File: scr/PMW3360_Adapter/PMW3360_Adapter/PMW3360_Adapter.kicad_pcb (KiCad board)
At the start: 2 copper layers, 11 parts, among them J1 Conn_01x06_Female, J2 Conn_01x02_Male, U1 TLV70019_SOT23-5, U2 PMW3360

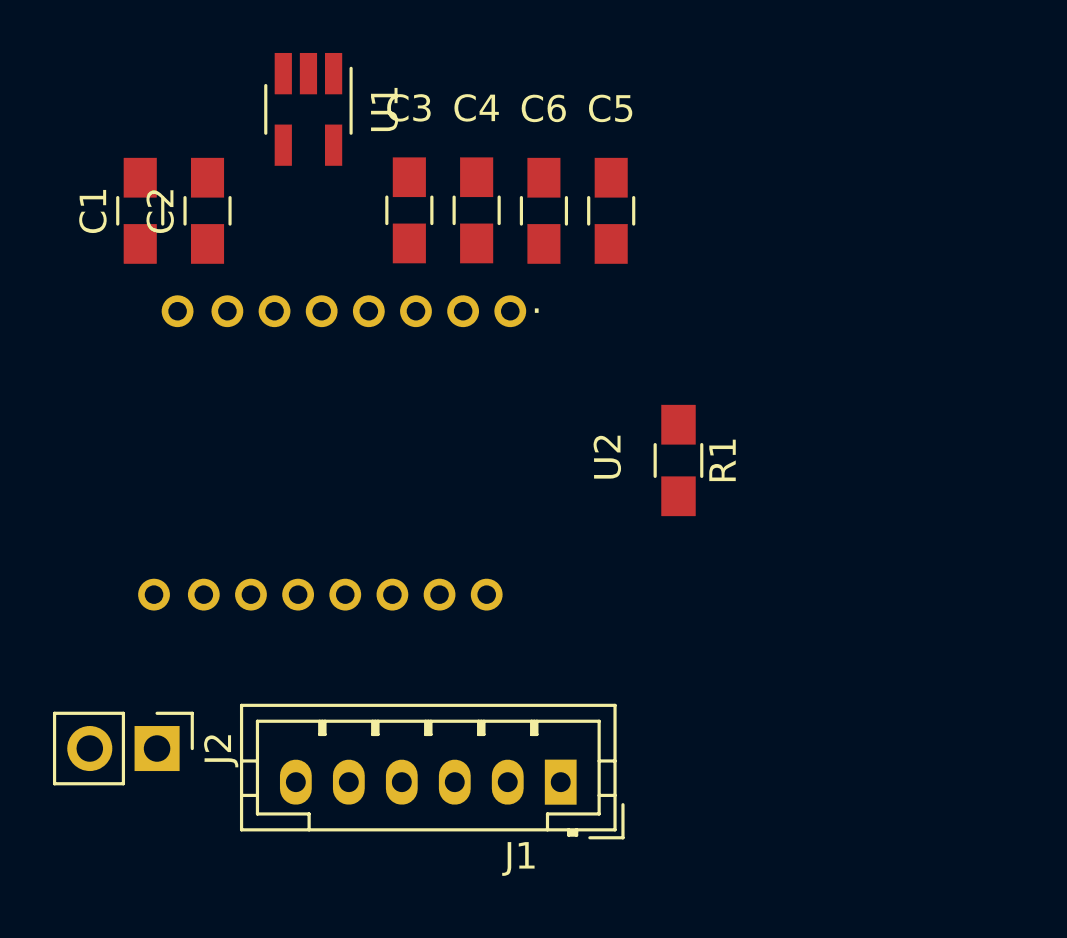
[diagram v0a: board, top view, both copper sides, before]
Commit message: PMW3360 Breakout ordered
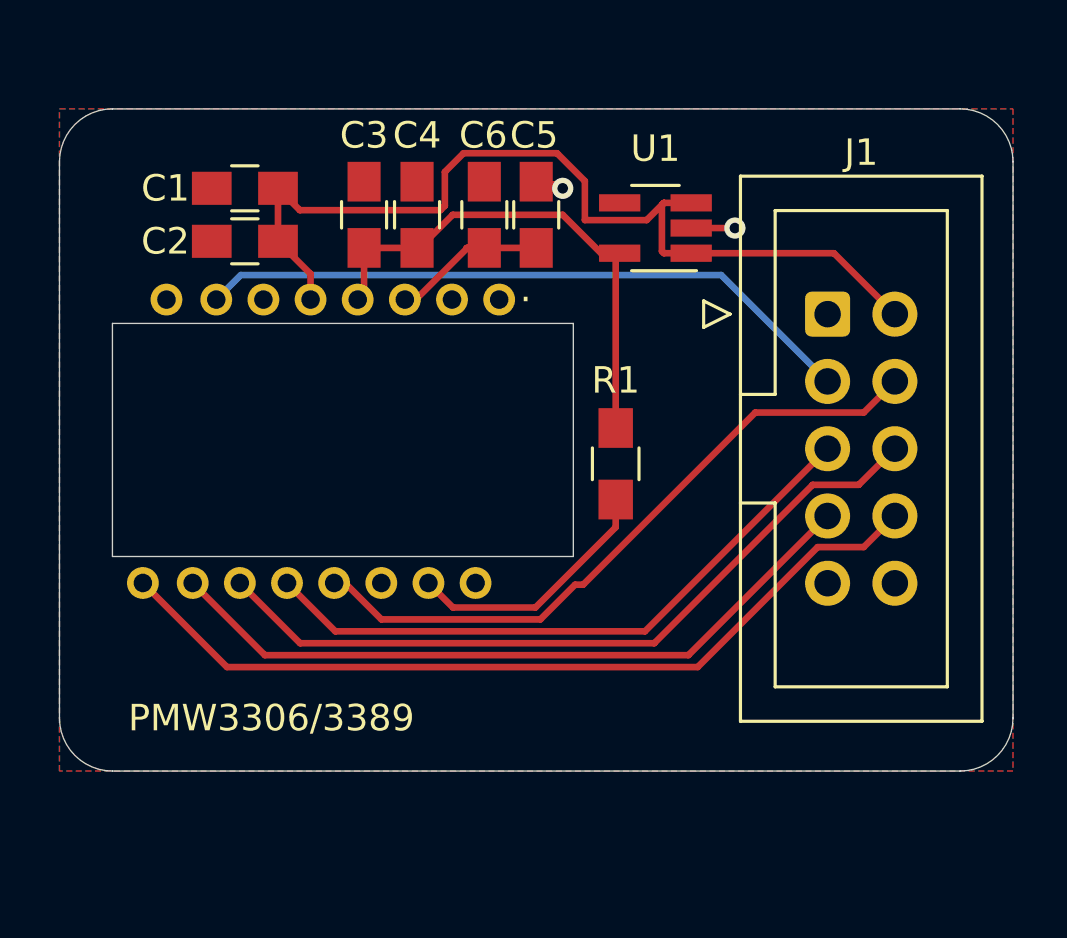
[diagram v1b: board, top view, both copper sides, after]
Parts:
- removed J2: Conn_01x02_Male, Pin_Headers:Pin_Header_Straight_1x02_Pitch2.54mm
- J1: value Conn_01x06_Female -> Conn_02x05_Odd_Even; footprint Connectors_JST:JST_PH_B6B-PH-K_06x2.00mm_Straight -> Connector_IDC:IDC-Header_2x05_P2.54mm_Vertical
- moved J1 20.3 mm to (108.5, 40.8), turned to 0 degrees
- moved U1 13.8 mm to (102.0, 37.5), turned to 180 degrees
- moved C1 4.04 mm to (86.5, 36.0), turned to 180 degrees
- moved C5 2.83 mm to (97.5, 37.0)
- moved R1 2.37 mm to (100.5, 46.4)
- moved C4 2.26 mm to (93.0, 37.0)
- moved C6 2.25 mm to (95.5, 37.0)
- moved C2 1.82 mm to (86.5, 38.0), turned to 180 degrees
- moved C3 1.72 mm to (91.0, 37.0)
- moved U2 0.61 mm to (96.1, 40.2)
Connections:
- J1 pad 3: ~CS -> ~RST
- J1 pad 4: MOSI -> ~CS
- J1 pad 6: SCLK -> MOSI
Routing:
- net +3V3: track 0.00 -> 36.1 mm
- net MOTION: track 0.00 -> 32.1 mm
- net MOSI: track 0.00 -> 28.7 mm
- net SCLK: track 0.00 -> 27.3 mm
- net ~CS: track 0.00 -> 25.5 mm
- net ~RST: track 0.00 -> 25.1 mm
- net MISO: track 0.00 -> 24.0 mm
- net +1V8: track 0.00 -> 19.5 mm
- net Net-(R1-Pad2): track 0.00 -> 9.75 mm
- net Net-(C5-Pad1): track 0.00 -> 6.92 mm
- net GND: track 0.00 -> 2.71 mm, vias 0 -> 2
- added copper zone on B.Cu, net GND
- added copper zone on F.Cu, net GND
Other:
- board outline added: 36 x 25 mm
- board text added: "BVH - AB4EN 2020 - 06"
- board text added: "PMW3306/3389"
